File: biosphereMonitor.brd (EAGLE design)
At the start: 85 x 85 mm, 60 parts, among them IC1 XMEGA32A4AU, IC2 LM35, IC3 FT232RL, IC4 NE555D, IC5 SST25VF040, Q1 16Mhz, Q2 32kHz

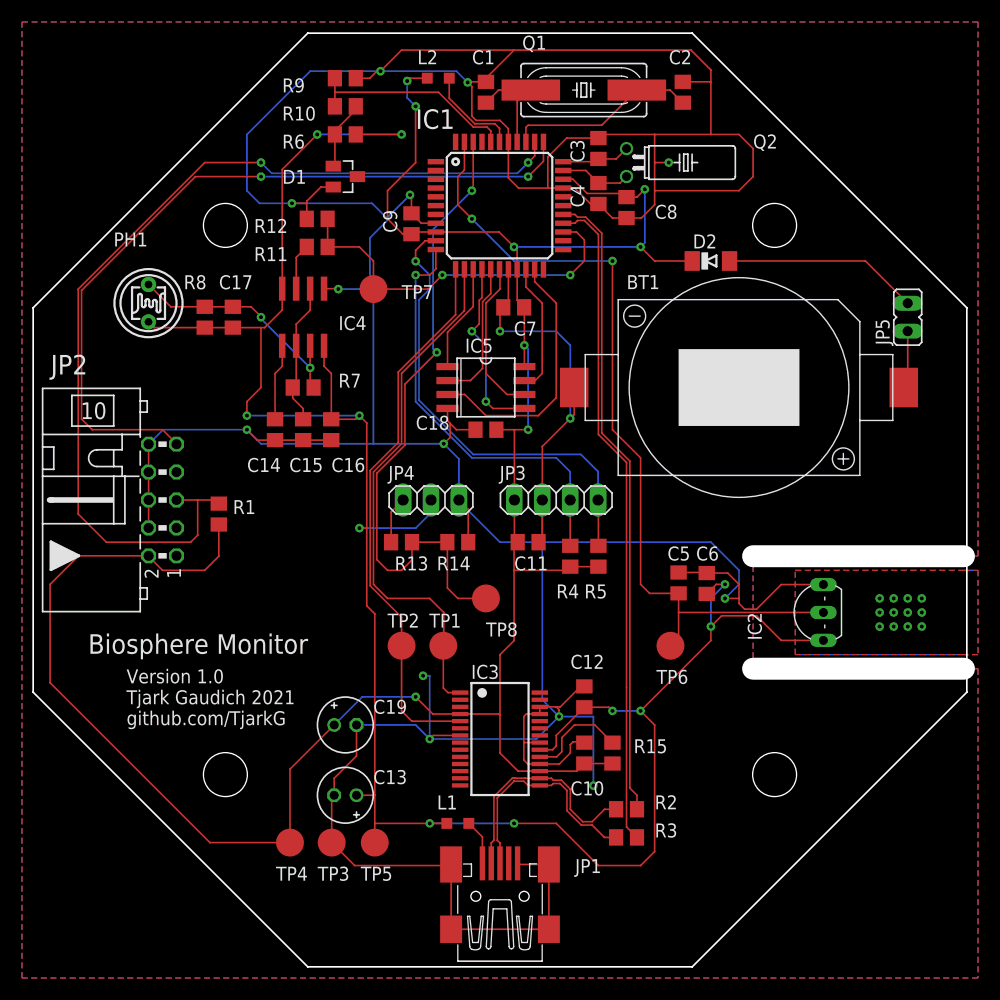
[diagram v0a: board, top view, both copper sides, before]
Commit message: added PCB options and cam file
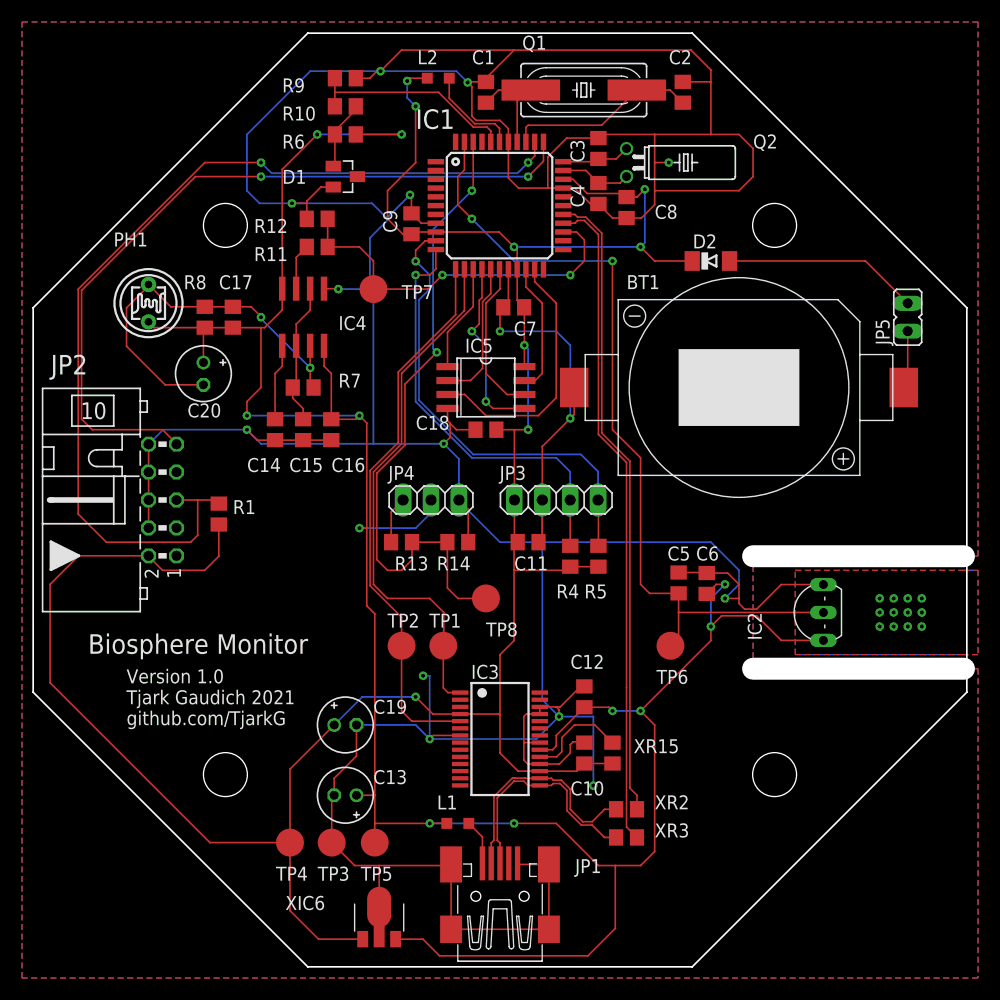
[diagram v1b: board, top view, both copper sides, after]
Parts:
- added C20: 4,7µF, rcl:E2-5
- added XIC6: 78L05F, linear:SOT89
- renumbered R15 to XR15, R2 to XR2, R3 to XR3
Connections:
- net +3V3: now also XIC6.1
- net +5V: now also C20.+, XIC6.3
- net GND: now also XIC6.2, XIC6.2@1
- net N$21: now also C20.-
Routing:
- net +5V: track 203.0 -> 233.5 mm
- net N$21: track 21.9 -> 36.8 mm
- net +3V3: track 216.9 -> 230.8 mm
- net GND: track 468.5 -> 474.9 mm
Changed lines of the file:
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@@
 <attribute name="VALUE" x="-24.32" y="-2.56" size="1.27" layer="27"/>
 </element>
-<element name="R2" library="rcl" library_urn="urn:adsk.eagle:library:334" package="R0805" package3d_urn="urn:adsk.eagle:package:23553/2" value="0" x="11.52" y="-28.16" smashed="yes">
+<element name="XR2" library="rcl" library_urn="urn:adsk.eagle:library:334" package="R0805" package3d_urn="urn:adsk.eagle:package:23553/2" value="0" x="11.52" y="-28.16" smashed="yes">
 <attribute name="NAME" x="14.08" y="-28.16" size="1.27" layer="25"/>
 <attribute name="POPULARITY" value="86" x="48.35" y="-82.77" size="1.778" layer="27" display="off"/>
 <attribute name="SPICEPREFIX" value="R" x="48.35" y="-82.77" size="1.778" layer="27" display="off"/>
 </element>
-<element name="R3" library="rcl" library_urn="urn:adsk.eagle:library:334" package="R0805" package3d_urn="urn:adsk.eagle:package:23553/2" value="0" x="11.52" y="-30.72" smashed="yes">
+<element name="XR3" library="rcl" library_urn="urn:adsk.eagle:library:334" package="R0805" package3d_urn="urn:adsk.eagle:package:23553/2" value="0" x="11.52" y="-30.72" smashed="yes">
 <attribute name="NAME" x="14.08" y="-30.72" size="1.27" layer="25"/>
 <attribute name="POPULARITY" value="86" x="53.43" y="-85.33" size="1.778" layer="27" display="off"/>
@@
 <attribute name="POPULARITY" value="86" x="-26.88" y="16.64" size="1.778" layer="27" rot="R90" display="off"/>
 <attribute name="SPICEPREFIX" value="R" x="-26.88" y="16.64" size="1.778" layer="27" rot="R90" display="off"/>
-<attribute name="VALUE" x="-28.795" y="12.82" size="1.27" layer="27"/>
+<attribute name="VALUE" x="-30.795" y="13.82" size="1.27" layer="27"/>
 </element>
 <element name="R11" library="rcl" library_urn="urn:adsk.eagle:library:334" package="R0805" package3d_urn="urn:adsk.eagle:package:23553/2" value="10k" x="-16.64" y="23.04" smashed="yes" rot="R180">
@@
 <attribute name="POPULARITY" value="25" x="19.2" y="21.76" size="1.778" layer="27" display="off"/>
 </element>
-<element name="R15" library="rcl" library_urn="urn:adsk.eagle:library:334" package="R0805" package3d_urn="urn:adsk.eagle:package:23553/2" value="10k" x="10.24" y="-23.04" smashed="yes" rot="R90">
+<element name="XR15" library="rcl" library_urn="urn:adsk.eagle:library:334" package="R0805" package3d_urn="urn:adsk.eagle:package:23553/2" value="10k" x="10.24" y="-23.04" smashed="yes" rot="R90">
 <attribute name="NAME" x="12.165" y="-23.05" size="1.27" layer="25"/>
 <attribute name="POPULARITY" value="86" x="10.24" y="-23.04" size="1.778" layer="27" rot="R90" display="off"/>
@@
 <attribute name="VALUE" x="-11.54" y="-22.639" size="1.27" layer="27" ratio="10"/>
 </element>
+<element name="XIC6" library="linear" library_urn="urn:adsk.eagle:library:262" package="SOT89" package3d_urn="urn:adsk.eagle:package:16478/2" value="78L05F" x="-11" y="-38" smashed="yes">
+<attribute name="NAME" x="-19.54" y="-37.325" size="1.27" layer="25"/>
+<attribute name="POPULARITY" value="5" x="-11" y="-38" size="1.778" layer="27" display="off"/>
+<attribute name="VALUE" x="-19.4051" y="-38.8449" size="1.27" layer="27"/>
+</element>
+<element name="C20" library="rcl" library_urn="urn:adsk.eagle:library:334" package="E2-5" package3d_urn="urn:adsk.eagle:package:23346/2" value="4,7µF" x="-27" y="11.5" smashed="yes" rot="R270">
+<attribute name="NAME" x="-28.46" y="7.516" size="1.27" layer="25" ratio="10"/>
+<attribute name="POPULARITY" value="14" x="-27" y="11.5" size="1.778" layer="27" rot="R270" display="off"/>
+<attribute name="SPICEPREFIX" value="C" x="-27" y="11.5" size="1.778" layer="27" rot="R270" display="off"/>
+<attribute name="VALUE" x="-28.46" y="5.841" size="1.27" layer="27" ratio="10"/>
+</element>
 </elements>
 <signals>
 <signal name="USB_MC_D_P">
 <contactref element="IC1" pad="26"/>
-<contactref element="R3" pad="2"/>
+<contactref element="XR3" pad="2"/>
 <wire x1="5.76" y1="25.2" x2="6.8148" y2="25.2" width="0.1524" layer="1"/>
 <wire x1="6.8148" y1="25.2" x2="7.0624" y2="25.4476" width="0.1524" layer="1"/>
@@
 <signal name="USB_MC_D_N">
 <contactref element="IC1" pad="27"/>
-<contactref element="R2" pad="2"/>
+<contactref element="XR2" pad="2"/>
 <wire x1="5.76" y1="26" x2="6.8148" y2="26" width="0.1524" layer="1"/>
 <wire x1="6.8148" y1="26" x2="7.0624" y2="25.7524" width="0.1524" layer="1"/>
@@
 <contactref element="D2" pad="C"/>
 <contactref element="IC3" pad="17"/>
-<contactref element="R15" pad="1"/>
+<contactref element="XR15" pad="1"/>
 <contactref element="IC3" pad="4"/>
 <contactref element="C19" pad="+"/>
@@
 <wire x1="-8.836" y1="24.196" x2="-8.06" y2="24.196" width="0.1524" layer="1"/>
 <wire x1="-10.24" y1="25.6" x2="-8.836" y2="24.196" width="0.1524" layer="1"/>
+<contactref element="XIC6" pad="1"/>
+<wire x1="-12.499" y1="-39.981" x2="-16.519" y2="-39.981" width="0.1524" layer="1"/>
+<wire x1="-19.12" y1="-37.38" x2="-19.12" y2="-31.19" width="0.1524" layer="1"/>
+<wire x1="-16.519" y1="-39.981" x2="-19.12" y2="-37.38" width="0.1524" layer="1"/>
 </signal>
 <signal name="GND">
@@
 <wire x1="-4.45" y1="-39.08" x2="4.45" y2="-39.08" width="0.1524" layer="1"/>
 <wire x1="-13.23" y1="-33.28" x2="-15.32" y2="-31.19" width="0.1524" layer="1"/>
-<wire x1="-4.45" y1="-33.28" x2="-13.23" y2="-33.28" width="0.1524" layer="1"/>
+<wire x1="-4.45" y1="-33.28" x2="-11" y2="-33.28" width="0.1524" layer="1"/>
+<wire x1="-11" y1="-33.28" x2="-13.23" y2="-33.28" width="0.1524" layer="1"/>
 <wire x1="-15.32" y1="-31.19" x2="-15.32" y2="-27.104" width="0.1524" layer="1"/>
 <wire x1="-15.32" y1="-27.104" x2="-15.096" y2="-26.88" width="0.1524" layer="1"/>
@@
 <wire x1="8.5" y1="-19.712" x2="8.5" y2="-26" width="0.1524" layer="16"/>
 <via x="8.5" y="-26" extent="1-16" drill="0.35"/>
+<contactref element="XIC6" pad="2"/>
+<contactref element="XIC6" pad="2@1"/>
+<wire x1="-11" y1="-39.727" x2="-11" y2="-37.06" width="0.1524" layer="1"/>
+<wire x1="-11" y1="-37.06" x2="-11" y2="-33.28" width="0.1524" layer="1"/>
 </signal>
 <signal name="N$1">
@@
 <wire x1="-26.88" y1="15.69" x2="-24.32" y2="15.69" width="0.1524" layer="1"/>
 <wire x1="-32" y1="16.22" x2="-31.47" y2="15.69" width="0.1524" layer="1"/>
-<wire x1="-31.47" y1="15.69" x2="-26.88" y2="15.69" width="0.1524" layer="1"/>
+<wire x1="-31.47" y1="15.69" x2="-27" y2="15.69" width="0.1524" layer="1"/>
+<wire x1="-27" y1="15.69" x2="-26.88" y2="15.69" width="0.1524" layer="1"/>
 <wire x1="-24.32" y1="15.69" x2="-21.76" y2="15.69" width="0.1524" layer="1"/>
 <wire x1="-21.76" y1="15.69" x2="-21.43" y2="15.69" width="0.1524" layer="1"/>
@@
 <wire x1="12.8" y1="-19.2" x2="14.08" y2="-20.48" width="0.1524" layer="1"/>
 <wire x1="14.08" y1="-32" x2="12.8" y2="-33.28" width="0.1524" layer="1"/>
-<wire x1="12.8" y1="-33.28" x2="8.96" y2="-33.28" width="0.1524" layer="1"/>
+<wire x1="12.8" y1="-33.28" x2="10.5" y2="-33.28" width="0.1524" layer="1"/>
+<wire x1="10.5" y1="-33.28" x2="8.96" y2="-33.28" width="0.1524" layer="1"/>
 <wire x1="8.96" y1="-33.28" x2="5.12" y2="-29.44" width="0.1524" layer="1"/>
 <wire x1="5.12" y1="-29.44" x2="1.28" y2="-29.44" width="0.1524" layer="1"/>
@@
 <via x="-12.8" y="-2.56" extent="1-16" drill="0.35"/>
 <wire x1="-12.8" y1="-2.56" x2="-12.1296" y2="-2.56" width="0.1524" layer="1"/>
+<contactref element="XIC6" pad="3"/>
+<contactref element="C20" pad="+"/>
+<wire x1="-27" y1="12.516" x2="-27" y2="15.69" width="0.1524" layer="1"/>
+<wire x1="-9.501" y1="-39.981" x2="-7.019" y2="-39.981" width="0.1524" layer="1"/>
+<wire x1="-7.019" y1="-39.981" x2="-5.5" y2="-41.5" width="0.1524" layer="1"/>
+<wire x1="-5.5" y1="-41.5" x2="8" y2="-41.5" width="0.1524" layer="1"/>
+<wire x1="8" y1="-41.5" x2="10.5" y2="-39" width="0.1524" layer="1"/>
+<wire x1="10.5" y1="-39" x2="10.5" y2="-33.28" width="0.1524" layer="1"/>
 </signal>
 <signal name="D_N">
 <contactref element="JP1" pad="2"/>
-<contactref element="R2" pad="1"/>
+<contactref element="XR2" pad="1"/>
 <contactref element="IC3" pad="16"/>
 <wire x1="-0.8" y1="-33.08" x2="-0.8" y2="-31.2252" width="0.1524" layer="1"/>
@@
 <signal name="D_P">
 <contactref element="JP1" pad="3"/>
-<contactref element="R3" pad="1"/>
+<contactref element="XR3" pad="1"/>
 <contactref element="IC3" pad="15"/>
 <wire x1="0" y1="-33.08" x2="0" y2="-31.2252" width="0.1524" layer="1"/>
@@
 <wire x1="-24.32" y1="17.59" x2="-26.88" y2="17.59" width="0.1524" layer="1"/>
 <wire x1="-26.88" y1="17.59" x2="-29.97" y2="17.59" width="0.1524" layer="1"/>
-<wire x1="-29.97" y1="17.59" x2="-32" y2="19.62" width="0.1524" layer="1"/>
+<wire x1="-29.97" y1="17.59" x2="-31.94" y2="19.56" width="0.1524" layer="1"/>
+<wire x1="-31.94" y1="19.56" x2="-32" y2="19.62" width="0.1524" layer="1"/>
 <wire x1="-24.32" y1="17.59" x2="-22.656" y2="17.59" width="0.1524" layer="1"/>
 <wire x1="-21.76" y1="16.64" x2="-21.76" y2="16.694" width="0.1524" layer="1"/>
@@
 <wire x1="-21.76" y1="16.507" x2="-17.285" y2="12.032" width="0.1524" layer="16"/>
 <via x="-17.285" y="12.032" extent="1-16" drill="0.35"/>
+<contactref element="C20" pad="-"/>
+<wire x1="-27" y1="10.484" x2="-30.484" y2="10.484" width="0.1524" layer="1"/>
+<wire x1="-30.484" y1="10.484" x2="-34" y2="14" width="0.1524" layer="1"/>
+<wire x1="-34" y1="14" x2="-34" y2="17.5" width="0.1524" layer="1"/>
+<wire x1="-34" y1="17.5" x2="-31.94" y2="19.56" width="0.1524" layer="1"/>
 </signal>
 <signal name="N$22">
@@
 </signal>
 <signal name="N$28">
-<contactref element="R15" pad="2"/>
+<contactref element="XR15" pad="2"/>
 <contactref element="IC3" pad="19"/>
 <wire x1="3.625" y1="-23.385" x2="5.159" y2="-23.385" width="0.1524" layer="1"/>

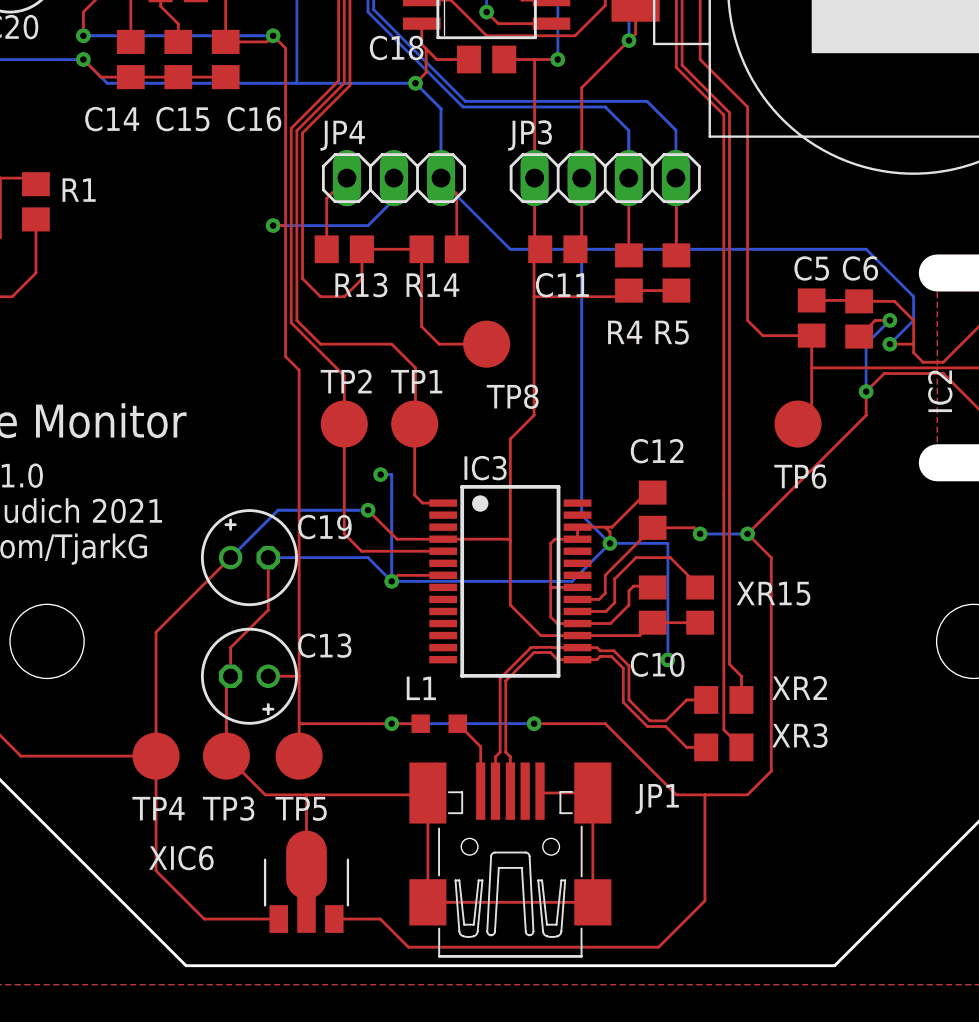
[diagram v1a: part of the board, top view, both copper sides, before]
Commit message: added option for external ftdi board
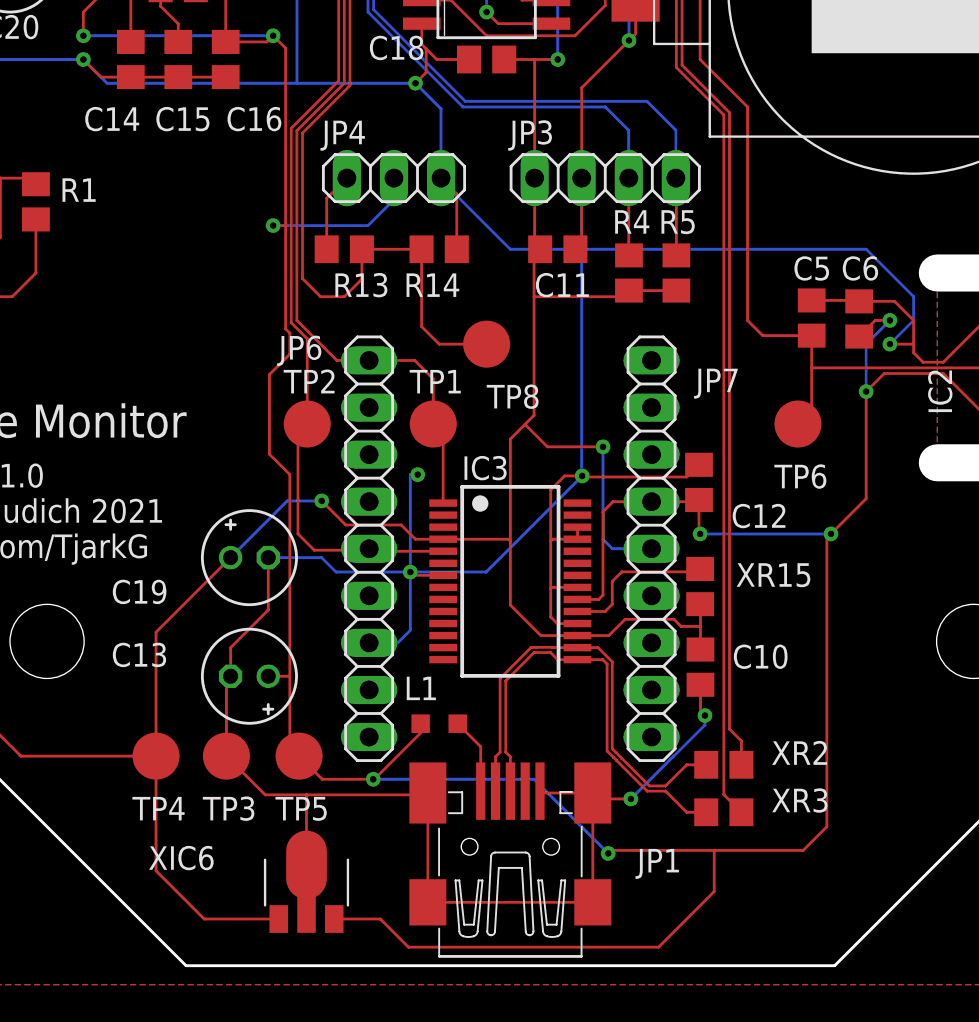
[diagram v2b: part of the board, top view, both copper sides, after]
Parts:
- added JP6, JP7: (no value), pinhead:1X09
- moved C10 4.23 mm to (10.3, -26.4), turned to 90 degrees
- moved XR2 3.50 mm to (11.5, -31.7)
- moved XR3 3.50 mm to (11.5, -34.2)
- moved C12 2.92 mm to (10.2, -16.4)
- moved TP2 2.00 mm to (-11.0, -13.3)
- moved TP1 1.00 mm to (-4.16, -13.3)
- moved XR15 1.00 mm to (10.2, -22.0)
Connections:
- net +3V3: now also JP7.5
- net +5V: now also JP7.4
- net GND: now also JP6.7
- net USB_RX: now also JP6.5
- net USB_TX: now also JP6.1
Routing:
- net +3V3: track 230.8 -> 246.5 mm, vias 8 -> 9
- net +5V: track 233.5 -> 246.8 mm
- net USB_MC_D_N: track 58.0 -> 61.5 mm
- net USB_MC_D_P: track 60.2 -> 63.7 mm
- net D_N: track 21.2 -> 24.3 mm
- net D_P: track 20.8 -> 23.8 mm
- net USB_RX: track 50.3 -> 52.3 mm
- net USB_TX: track 49.0 -> 47.7 mm
- net N$28: track 9.23 -> 8.29 mm
- net GND: track 474.9 -> 475.1 mm, vias 15 -> 16
